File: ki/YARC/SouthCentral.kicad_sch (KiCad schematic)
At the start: 9 parts, among them U104 74LS86, U83 74LS139, U84 74LS157, U85 74LS157, U86 74LS157, U87 74LS138, U88 74HC00, U89 74LS157, U90 74LS157

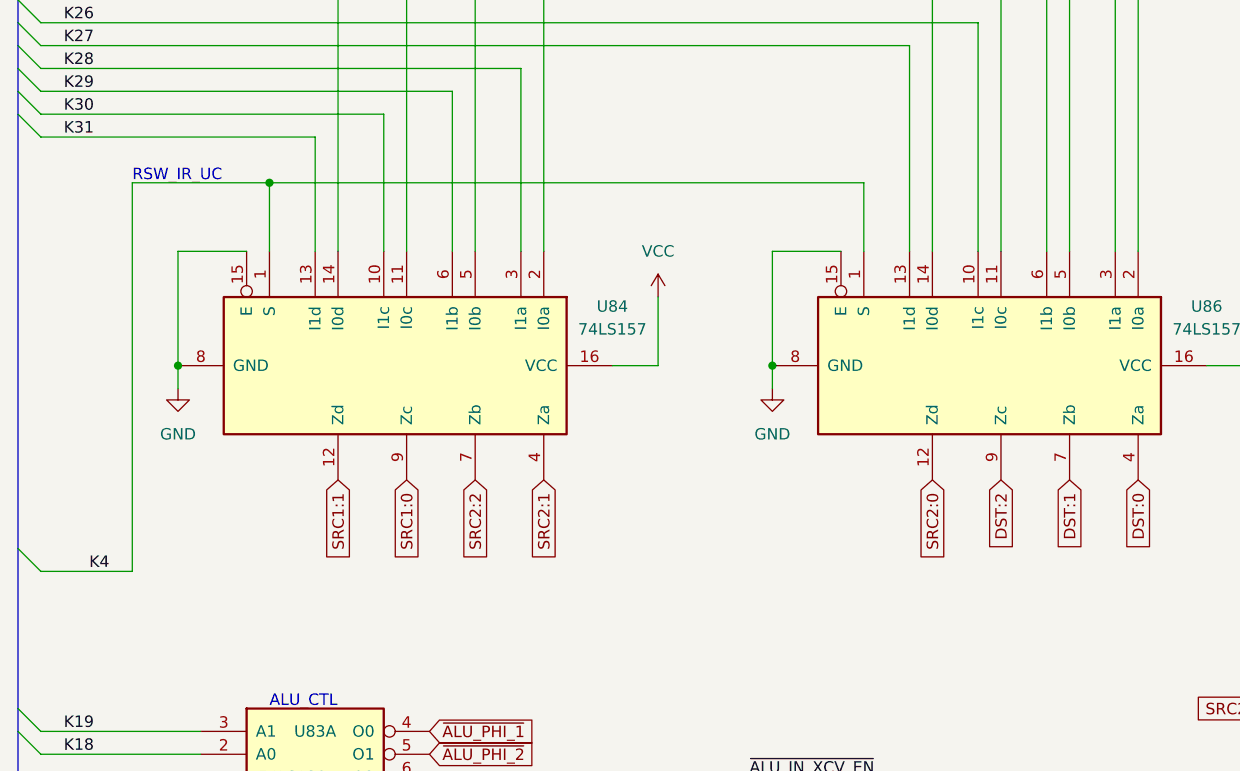
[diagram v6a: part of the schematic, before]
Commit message: Additional minor corrections. ERC clean.
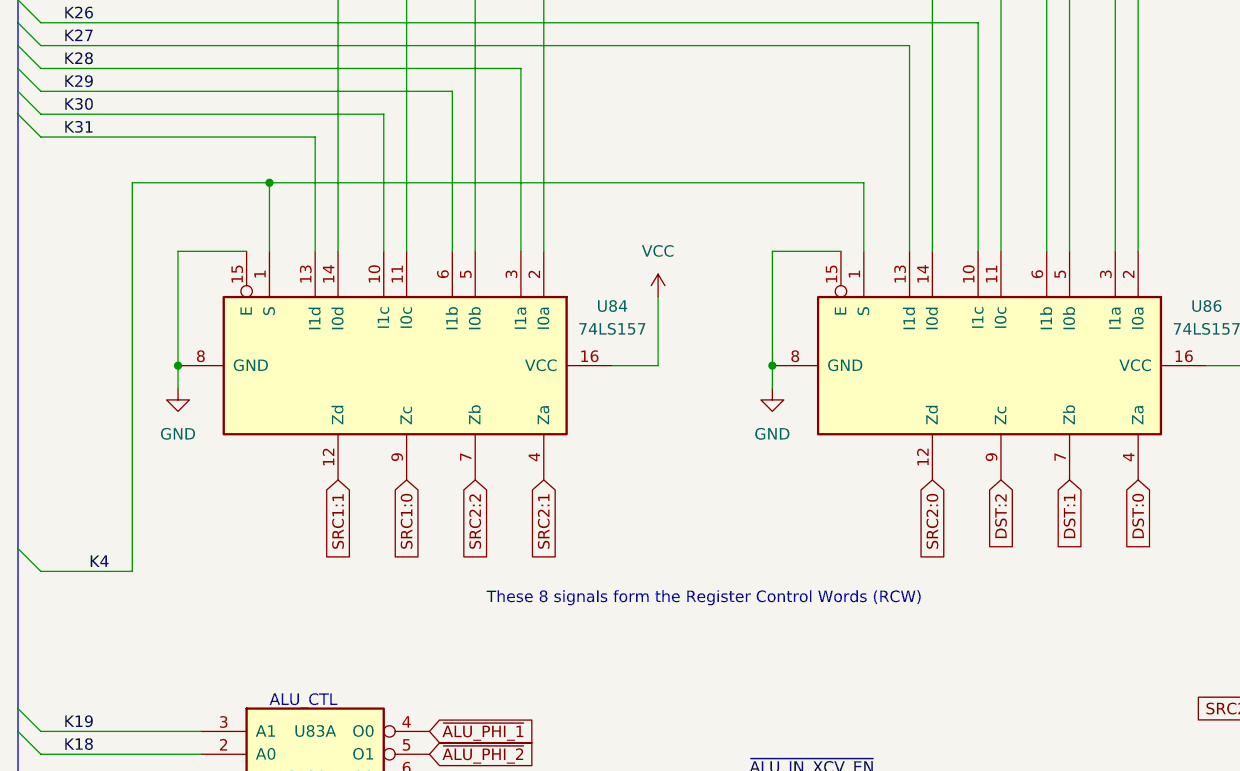
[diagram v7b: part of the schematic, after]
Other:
- note added: "These 8 signals form the Register Control Words (RCW)"
- note removed: "RSW_IR_UC"
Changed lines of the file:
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@@
+    (effects (font (size 1.27 1.27)) (justify left bottom))
+  )
+  (text "These 8 signals form the Register Control Words (RCW)"
+    (at 67.31 102.87 0)
     (effects (font (size 1.27 1.27)) (justify left bottom))
   )
@@
     (effects (font (size 1.27 1.27)) (justify left bottom))
   )
-  (text "RSW_IR_UC" (at 27.94 55.88 0)
-    (effects (font (size 1.27 1.27)) (justify left bottom))
-  )

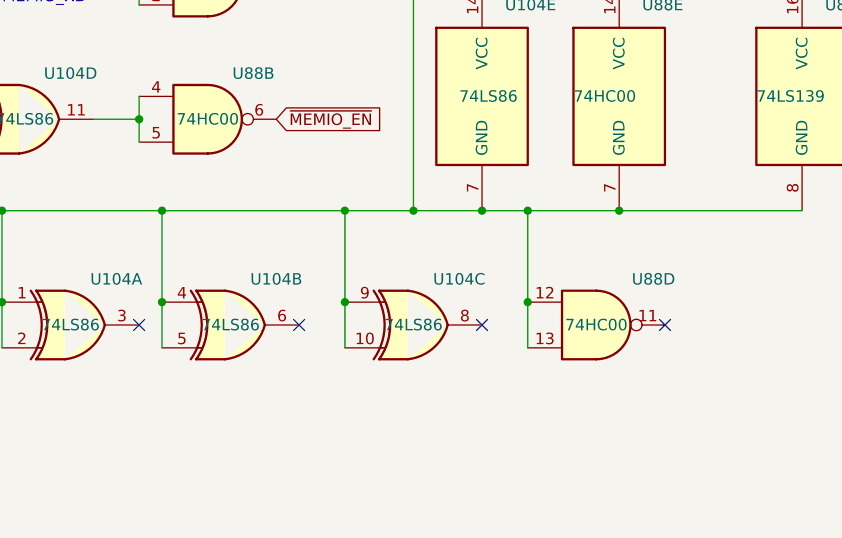
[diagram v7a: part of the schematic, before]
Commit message: Revise SET# logic for LD_UCODE_CTR#. Fix minor errors with no functional consequences (schematic didn't match reality)
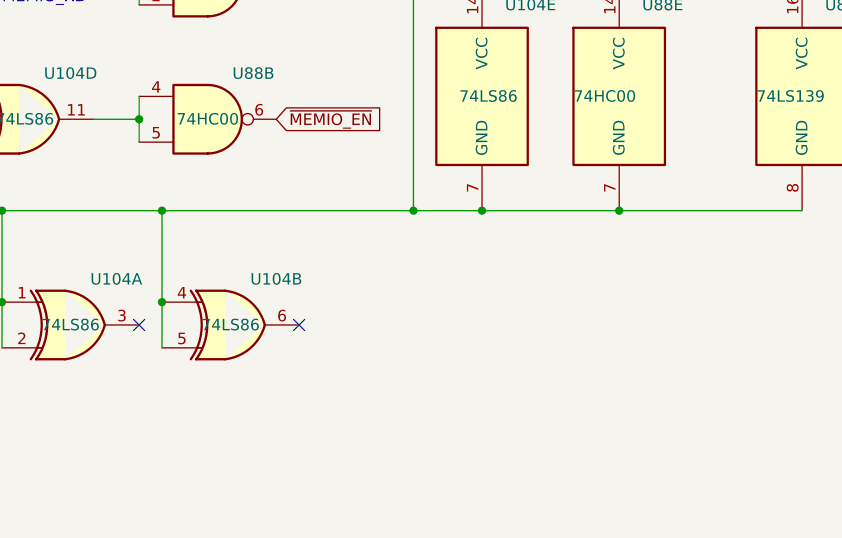
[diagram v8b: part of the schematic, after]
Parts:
- removed unit 3 of U104
- removed unit 4 of U88
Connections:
- no-connect marks 11 -> 9
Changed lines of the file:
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@@
   (junction (at 165.1 167.64) (diameter 0) (color 0 0 0 0)
   )
-  (junction (at 203.2 167.64) (diameter 0) (color 0 0 0 0)
-  )
   (junction (at 210.82 48.26) (diameter 0) (color 0 0 0 0)
   )
@@
   (junction (at 233.68 167.64) (diameter 0) (color 0 0 0 0)
   )
-  (junction (at 203.2 177.8) (diameter 0) (color 0 0 0 0)
-  )
   (junction (at 33.02 76.2) (diameter 0) (color 0 0 0 0)
   )
@@
   )
   (junction (at 165.1 177.8) (diameter 0) (color 0 0 0 0)
-  )
-  (junction (at 223.52 167.64) (diameter 0) (color 0 0 0 0)
-  )
-  (junction (at 223.52 177.8) (diameter 0) (color 0 0 0 0)
   )
   (junction (at 210.82 99.06) (diameter 0) (color 0 0 0 0)
@@
   (no_connect (at 238.76 99.06))
   (no_connect (at 195.58 71.12))
-  (no_connect (at 238.76 180.34))
   (no_connect (at 154.94 147.32))
   (no_connect (at 154.94 144.78))
   (no_connect (at 198.12 180.34))
   (no_connect (at 154.94 149.86))
-  (no_connect (at 218.44 180.34))
   (bus_entry (at 127 157.48) (size -2.54 2.54)
     (stroke (width 0) (type default))
@@
     (stroke (width 0) (type default))
   )
-  (wire (pts (xy 203.2 177.8) (xy 203.2 167.64))
-    (stroke (width 0) (type default))
-  )
   (wire (pts (xy 139.7 20.32) (xy 139.7 63.5))
     (stroke (width 0) (type default))
@@
     (stroke (width 0) (type default))
   )
-  (wire (pts (xy 223.52 182.88) (xy 223.52 177.8))
-    (stroke (width 0) (type default))
-  )
   (wire (pts (xy 200.66 50.8) (xy 213.36 50.8))
     (stroke (width 0) (type default))
@@
     (stroke (width 0) (type default))
   )
-  (wire (pts (xy 223.52 167.64) (xy 233.68 167.64))
-    (stroke (width 0) (type default))
-  )
   (wire (pts (xy 129.54 149.86) (xy 129.54 157.48))
     (stroke (width 0) (type default))
@@
     (stroke (width 0) (type default))
   )
-  (wire (pts (xy 223.52 177.8) (xy 223.52 167.64))
-    (stroke (width 0) (type default))
-  )
   (wire (pts (xy 129.54 63.5) (xy 129.54 35.56))
     (stroke (width 0) (type default))
@@
     (stroke (width 0) (type default))
   )
-  (wire (pts (xy 218.44 167.64) (xy 223.52 167.64))
+  (wire (pts (xy 218.44 167.64) (xy 233.68 167.64))
     (stroke (width 0) (type default))
   )
@@
     (stroke (width 0) (type default))
   )
-  (wire (pts (xy 203.2 167.64) (xy 210.82 167.64))
-    (stroke (width 0) (type default))
-  )
   (wire (pts (xy 205.74 132.08) (xy 205.74 121.92))
     (stroke (width 0) (type default))
@@
     (stroke (width 0) (type default))
   )
-  (wire (pts (xy 182.88 167.64) (xy 203.2 167.64))
+  (wire (pts (xy 182.88 167.64) (xy 210.82 167.64))
     (stroke (width 0) (type default))
   )
@@
   )
   (bus (pts (xy 15.24 182.88) (xy 15.24 187.96))
-    (stroke (width 0) (type default))
-  )
-  (wire (pts (xy 203.2 182.88) (xy 203.2 177.8))
     (stroke (width 0) (type default))
   )
@@
     )
   )
-  (symbol (lib_id "74xx:74LS86") (at 210.82 180.34 0) (unit 3)
-    (in_bom yes) (on_board yes) (dnp no)
-    (property "Reference" "U104" (at 215.9 175.26 0)
-      (effects (font (size 1.27 1.27)))
-    )
-    (property "Value" "74LS86" (at 210.82 180.34 0)
-      (effects (font (size 1.27 1.27)))
-    )
-    (property "Footprint" "" (at 210.82 180.34 0)
-      (effects (font (size 1.27 1.27)) hide)
-    )
-    (property "Datasheet" "74xx/74ls86.pdf" (at 210.82 180.34 0)
-      (effects (font (size 1.27 1.27)) hide)
-    )
-    (pin "1")
-    (pin "2")
-    (pin "3")
-    (pin "4")
-    (pin "5")
-    (pin "6")
-    (pin "10")
-    (pin "8")
-    (pin "9")
-    (pin "11")
-    (pin "12")
-    (pin "13")
-    (pin "14")
-    (pin "7")
-    (instances
-      (project "YARC"
-        (path "/22e0f8e1-b0d7-4d47-bb7c-8ef04cd95fca/89d830c1-f0d9-4d89-9863-428a1b54ae3d"
-          (reference "U104") (unit 3)
-        )
-      )
-    )
-  )
   (symbol (lib_id "power:VCC") (at 226.06 83.82 0) (unit 1)
     (in_bom yes) (on_board yes) (dnp no) (fields_autoplaced)
@@
         )
       )
-    )
-  )
-  (symbol (lib_id "74xx:74HC00") (at 231.14 180.34 0) (unit 4)
-    (in_bom yes) (on_board yes) (dnp no)
-    (property "Reference" "U88" (at 237.49 175.26 0)
-      (effects (font (size 1.27 1.27)))
-    )
-    (property "Value" "74HC00" (at 231.14 180.34 0)
-      (effects (font (size 1.27 1.27)))
-    )
-    (property "Footprint" "" (at 231.14 180.34 0)
-      (effects (font (size 1.27 1.27)) hide)
-    )
-    (property "Datasheet" "http://www.ti.com/lit/gpn/sn74hc00" (at 231.14 180.34 0)
-      (effects (font (size 1.27 1.27)) hide)
-    )
-    (pin "1")
-    (pin "2")
-    (pin "3")
-    (pin "4")
-    (pin "5")
-    (pin "6")
-    (pin "10")
-    (pin "8")
-    (pin "9")
-    (pin "11")
-    (pin "12")
-    (pin "13")
-    (pin "14")
-    (pin "7")
-    (instances
-      (project "YARC"
-        (path "/22e0f8e1-b0d7-4d47-bb7c-8ef04cd95fca/89d830c1-f0d9-4d89-9863-428a1b54ae3d"
-          (reference "U88") (unit 4)
-        )
-      )
